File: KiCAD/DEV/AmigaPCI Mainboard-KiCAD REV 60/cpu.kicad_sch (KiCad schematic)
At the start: 55 parts, among them CN200 DIN41612_03x40, CN712 SPI, U712 ICE40HX4K-TQ144, U712F1 W25X20CLSN, U814 74LVC245, U816 74LVC245, U817 74LVC245

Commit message: APCI Rev 6.0 Work
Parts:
- added R277, R278: 2k7, Resistor_SMD:R_0603_1608Metric, symbol Device:R
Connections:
- net +3V3: now also R277.1, R278.1
- net _TBI: now also R278.2
- net _TEA: now also R277.2
- net _AWEN: now reaches U712.119 (IO0_178)
- no-connect marks 4 -> 3
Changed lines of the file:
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@@
 	(title_block
 		(title "AMIGA PCI")
-		(date "2025-04-24")
+		(date "2025-04-28")
 		(rev "6.0")
 	)
@@
 	)
 	(junction
+		(at 386.08 68.58)
+		(diameter 0)
+		(color 0 0 0 0)
+	)
+	(junction
 		(at 68.58 213.36)
 		(diameter 0)
@@
 	)
 	(junction
+		(at 388.62 68.58)
+		(diameter 0)
+		(color 0 0 0 0)
+	)
+	(junction
 		(at 393.7 68.58)
 		(diameter 0)
@@
 	)
 	(no_connect
-		(at 134.62 187.96)
-	)
-	(no_connect
 		(at 74.93 50.8)
 	)
@@
 	(wire
 		(pts
+			(xy 383.54 68.58) (xy 386.08 68.58)
+		)
+		(stroke
+			(width 0)
+			(type default)
+		)
+	)
+	(wire
+		(pts
 			(xy 44.45 210.82) (xy 53.34 210.82)
 		)
@@
 	(wire
 		(pts
+			(xy 383.54 88.9) (xy 383.54 82.55)
+		)
+		(stroke
+			(width 0)
+			(type default)
+		)
+	)
+	(wire
+		(pts
 			(xy 74.93 142.24) (xy 66.04 142.24)
 		)
@@
 	(wire
 		(pts
+			(xy 386.08 88.9) (xy 386.08 82.55)
+		)
+		(stroke
+			(width 0)
+			(type default)
+		)
+	)
+	(wire
+		(pts
 			(xy 129.54 43.18) (xy 129.54 45.72)
 		)
@@
 	(wire
 		(pts
+			(xy 386.08 68.58) (xy 386.08 74.93)
+		)
+		(stroke
+			(width 0)
+			(type default)
+		)
+	)
+	(wire
+		(pts
 			(xy 66.04 139.7) (xy 74.93 139.7)
 		)
@@
 	(wire
 		(pts
+			(xy 383.54 68.58) (xy 383.54 74.93)
+		)
+		(stroke
+			(width 0)
+			(type default)
+		)
+	)
+	(wire
+		(pts
 			(xy 312.42 157.48) (xy 311.15 157.48)
 		)
@@
 		)
 	)
+	(wire
+		(pts
+			(xy 386.08 68.58) (xy 388.62 68.58)
+		)
+		(stroke
+			(width 0)
+			(type default)
+		)
+	)
 	(bus
 		(pts
@@
 		)
 	)
+	(label "_TBI"
+		(at 383.54 88.9 90)
+		(effects
+			(font
+				(size 1.27 1.27)
+			)
+			(justify left bottom)
+		)
+	)
 	(label "D21"
 		(at 303.53 92.71 0)
@@
 		)
 	)
+	(label "_TEA"
+		(at 386.08 88.9 90)
+		(effects
+			(font
+				(size 1.27 1.27)
+			)
+			(justify left bottom)
+		)
+	)
 	(label "A23"
 		(at 328.93 57.15 0)
@@
 		)
 	)
+	(global_label "_AWEN"
+		(shape output)
+		(at 134.62 187.96 0)
+		(fields_autoplaced yes)
+		(effects
+			(font
+				(size 1.27 1.27)
+			)
+			(justify left)
+		)
+		(property "Intersheetrefs" "${INTERSHEET_REFS}"
+			(at 143.5923 187.96 0)
+			(effects
+				(font
+					(size 1.27 1.27)
+				)
+				(justify left)
+			)
+		)
+	)
 	(global_label "_BUSREQ1"
 		(shape output)
@@
 	)
 	(symbol
+		(lib_id "Device:R")
+		(at 386.08 78.74 0)
+		(mirror y)
+		(unit 1)
+		(exclude_from_sim no)
+		(in_bom yes)
+		(on_board yes)
+		(dnp no)
+		(property "Reference" "R277"
+			(at 384.81 75.692 90)
+			(effects
+				(font
+					(size 1.27 1.27)
+				)
+				(justify left)
+			)
+		)
+		(property "Value" "2k7"
+			(at 386.08 80.772 90)
+			(effects
+				(font
+					(size 1.27 1.27)
+				)
+				(justify left)
+			)
+		)
+		(property "Footprint" "Resistor_SMD:R_0603_1608Metric"
+			(at 387.858 78.74 90)
+			(effects
+				(font
+					(size 1.27 1.27)
+				)
+				(hide yes)
+			)
+		)
+		(property "Datasheet" "~"
+			(at 386.08 78.74 0)
+			(effects
+				(font
+					(size 1.27 1.27)
+				)
+				(hide yes)
+			)
+		)
+		(property "Description" ""
+			(at 386.08 78.74 0)
+			(effects
+				(font
+					(size 1.27 1.27)
+				)
+				(hide yes)
+			)
+		)
+		(pin "1"
+		)
+		(pin "2"
+		)
+		(instances
+			(project "AmigaPCI Mainboard"
+				(path "/72453515-27fe-4336-91f3-e3c8054f7767/14024e2c-eaac-4547-8875-4a8ac58b1720"
+					(reference "R277")
+					(unit 1)
+				)
+			)
+		)
+	)
+	(symbol
 		(lib_id "Device:R_Network08")
 		(at 339.09 90.17 270)
@@
 					(unit 1)
 				)
+			)
+		)
+	)
+	(symbol
+		(lib_id "Device:R")
+		(at 383.54 78.74 0)
+		(mirror y)
+		(unit 1)
+		(exclude_from_sim no)
+		(in_bom yes)
+		(on_board yes)
+		(dnp no)
+		(property "Reference" "R278"
+			(at 382.27 75.692 90)
+			(effects
+				(font
+					(size 1.27 1.27)
+				)
+				(justify left)
+			)
+		)
+		(property "Value" "2k7"
+			(at 383.54 80.772 90)
+			(effects
+				(font
+					(size 1.27 1.27)
+				)
+				(justify left)
+			)
+		)
+		(property "Footprint" "Resistor_SMD:R_0603_1608Metric"
+			(at 385.318 78.74 90)
+			(effects
+				(font
+					(size 1.27 1.27)
+				)
+				(hide yes)
+			)
+		)
+		(property "Datasheet" "~"
+			(at 383.54 78.74 0)
+			(effects
+				(font
+					(size 1.27 1.27)
+				)
+				(hide yes)
+			)
+		)
+		(property "Description" ""
+			(at 383.54 78.74 0)
+			(effects
+				(font
+					(size 1.27 1.27)
+				)
+				(hide yes)
+			)
+		)
+		(pin "1"
+		)
+		(pin "2"
+		)
+		(instances
+			(project "AmigaPCI Mainboard"
+				(path "/72453515-27fe-4336-91f3-e3c8054f7767/14024e2c-eaac-4547-8875-4a8ac58b1720"
+					(reference "R278")
+					(unit 1)
+				)

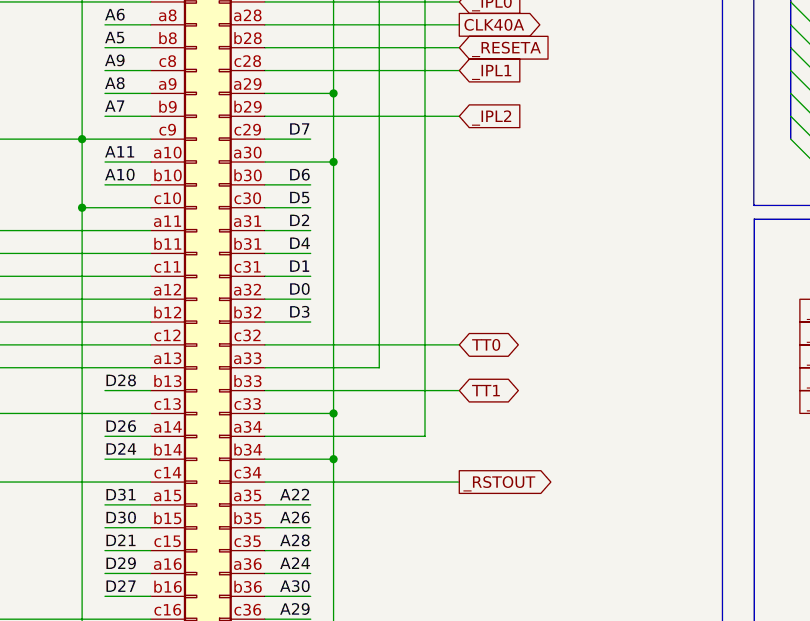
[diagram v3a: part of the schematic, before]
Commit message: Rev 6.0 APCI Work
Added ATA address lines to U110.
Cleaned up some routing.
Removed address lines from U109 - we can pick them up from the AD bus.
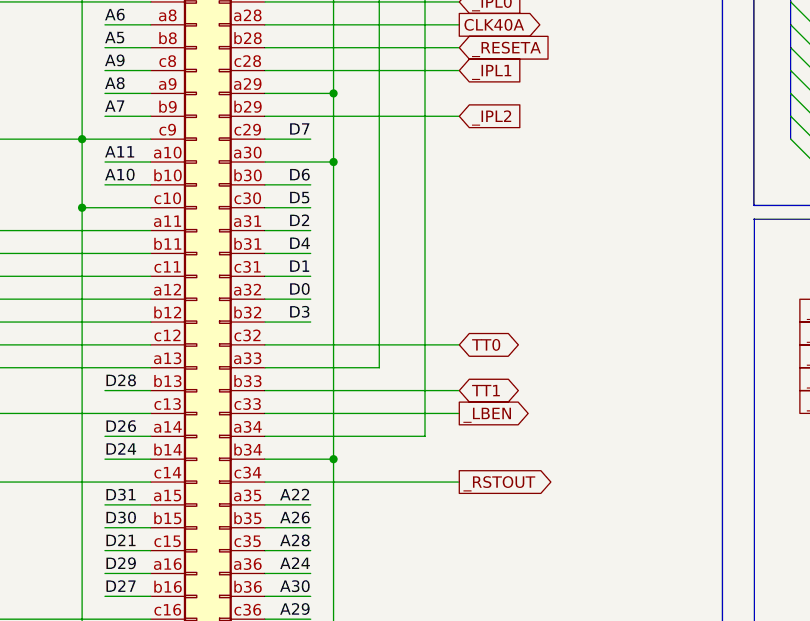
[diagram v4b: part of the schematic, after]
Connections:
- net GND: no longer CN200.c33 (Pin_c33)
- new net _LBEN: CN200.c33 (Pin_c33)
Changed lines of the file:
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@@
 	)
 	(junction
-		(at 250.19 146.05)
-		(diameter 0)
-		(color 0 0 0 0)
-	)
-	(junction
 		(at 375.92 38.1)
 		(diameter 0)
@@
 	(wire
 		(pts
-			(xy 250.19 146.05) (xy 250.19 151.13)
-		)
-		(stroke
-			(width 0)
-			(type default)
-		)
-	)
-	(wire
-		(pts
 			(xy 134.62 195.58) (xy 125.73 195.58)
 		)
@@
 	(wire
 		(pts
-			(xy 250.19 118.11) (xy 250.19 146.05)
+			(xy 250.19 118.11) (xy 250.19 151.13)
 		)
 		(stroke
@@
 	(wire
 		(pts
+			(xy 242.57 146.05) (xy 264.16 146.05)
+		)
+		(stroke
+			(width 0)
+			(type default)
+		)
+	)
+	(wire
+		(pts
 			(xy 134.62 180.34) (xy 125.73 180.34)
 		)
@@
 	(wire
 		(pts
-			(xy 242.57 146.05) (xy 250.19 146.05)
-		)
-		(stroke
-			(width 0)
-			(type default)
-		)
-	)
-	(wire
-		(pts
 			(xy 163.83 76.2) (xy 163.83 83.82)
 		)
@@
 			(effects
 				(font
+					(size 1.27 1.27)
+				)
+				(justify left)
+			)
+		)
+	)
+	(global_label "_LBEN"
+		(shape output)
+		(at 264.16 146.05 0)
+		(fields_autoplaced yes)
+		(effects
+			(font
+				(size 1.27 1.27)
+			)
+			(justify left)
+		)
+		(property "Intersheetrefs" "${INTERSHEET_REFS}"
+			(at 272.8904 146.05 0)
+			(effects
+				(font

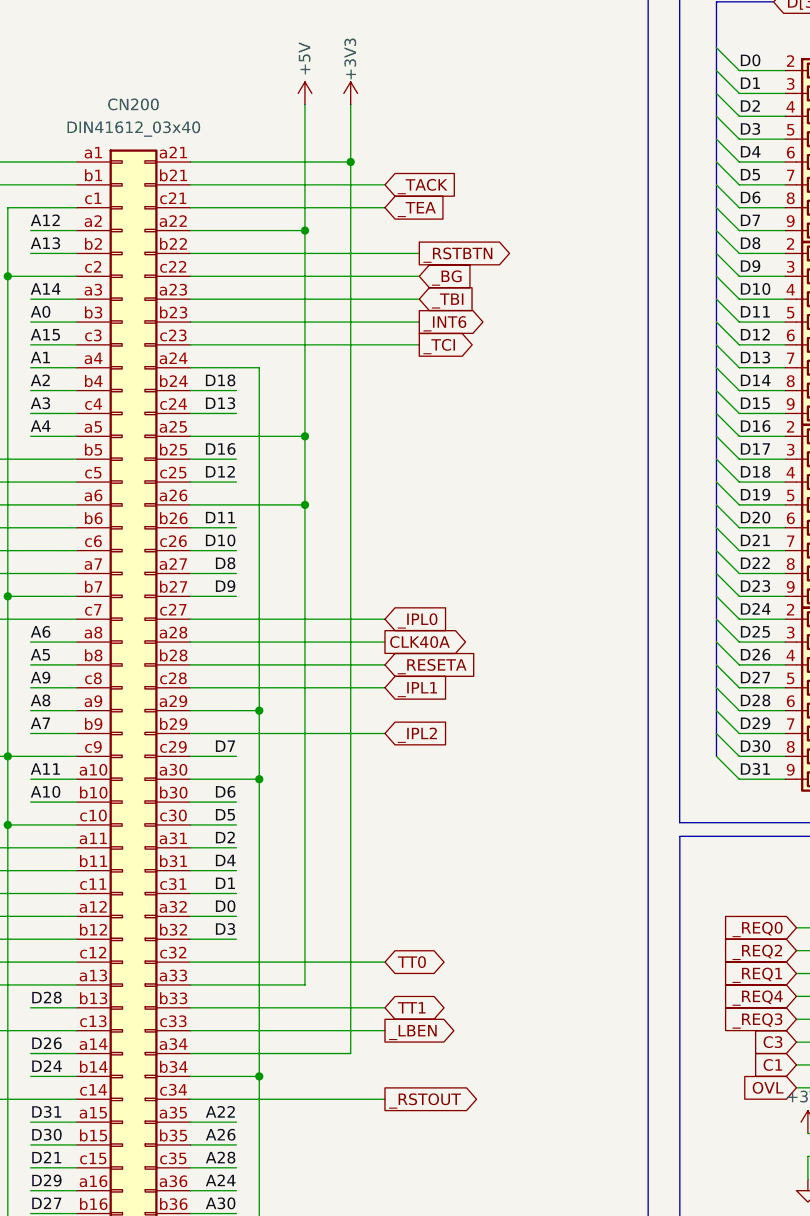
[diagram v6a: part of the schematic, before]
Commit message: APCI Added _LBEN pullup.
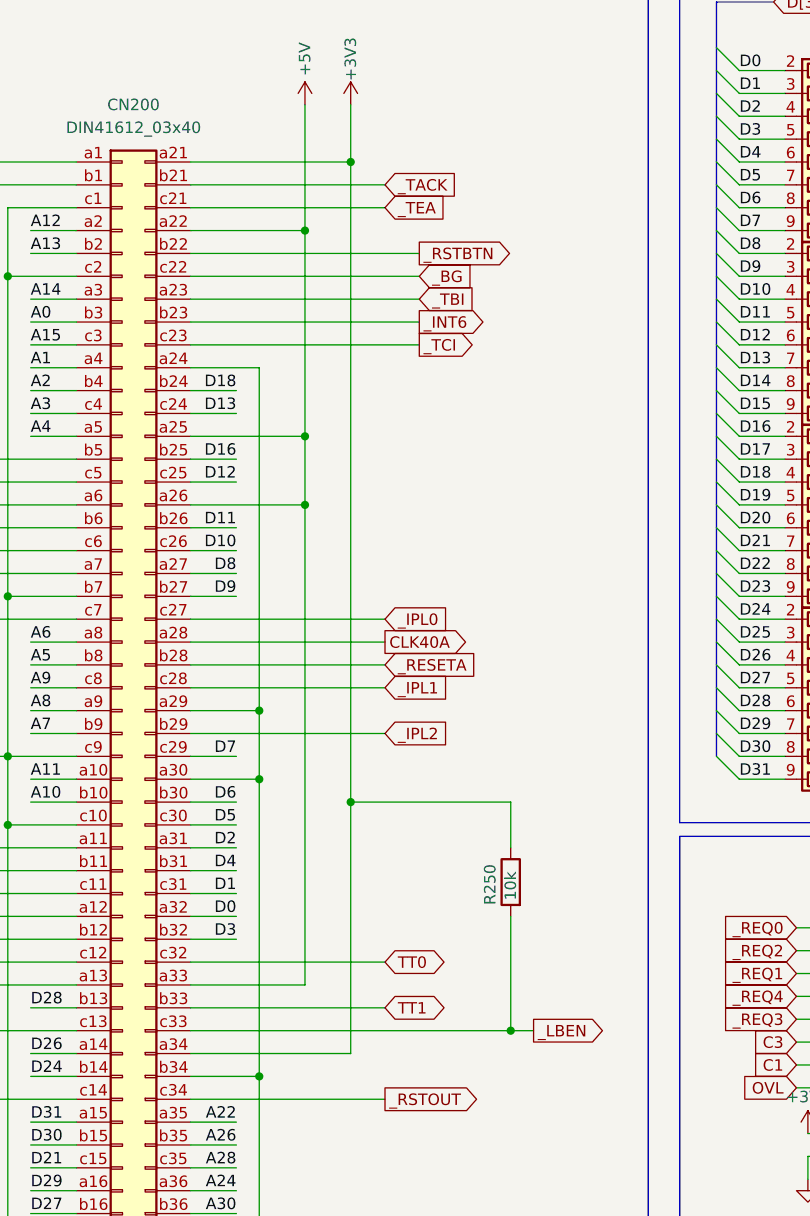
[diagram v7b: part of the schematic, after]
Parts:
- added R250: 10k, Resistor_SMD:R_0603_1608Metric, symbol Device:R
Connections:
- net +3V3: now also R250.1
- net _LBEN: now also R250.2
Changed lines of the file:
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@@
 	)
 	(junction
+		(at 260.35 120.65)
+		(diameter 0)
+		(color 0 0 0 0)
+	)
+	(junction
 		(at 151.13 50.8)
 		(diameter 0)
@@
 	)
 	(junction
+		(at 278.13 146.05)
+		(diameter 0)
+		(color 0 0 0 0)
+	)
+	(junction
 		(at 68.58 213.36)
 		(diameter 0)
@@
 		)
 	)
+	(wire
+		(pts
+			(xy 278.13 133.35) (xy 278.13 146.05)
+		)
+		(stroke
+			(width 0)
+			(type default)
+		)
+	)
 	(bus
 		(pts
@@
 	(wire
 		(pts
-			(xy 260.35 49.53) (xy 260.35 148.59)
+			(xy 260.35 49.53) (xy 260.35 120.65)
 		)
 		(stroke
@@
 	(wire
 		(pts
+			(xy 278.13 146.05) (xy 280.67 146.05)
+		)
+		(stroke
+			(width 0)
+			(type default)
+		)
+	)
+	(wire
+		(pts
 			(xy 242.57 118.11) (xy 250.19 118.11)
 		)
@@
 		)
 	)
+	(wire
+		(pts
+			(xy 278.13 125.73) (xy 278.13 120.65)
+		)
+		(stroke
+			(width 0)
+			(type default)
+		)
+	)
 	(bus
 		(pts
@@
 	(wire
 		(pts
+			(xy 260.35 120.65) (xy 260.35 148.59)
+		)
+		(stroke
+			(width 0)
+			(type default)
+		)
+	)
+	(wire
+		(pts
 			(xy 334.01 118.11) (xy 328.93 118.11)
 		)
@@
 	(wire
 		(pts
+			(xy 260.35 120.65) (xy 278.13 120.65)
+		)
+		(stroke
+			(width 0)
+			(type default)
+		)
+	)
+	(wire
+		(pts
 			(xy 242.57 87.63) (xy 255.27 87.63)
 		)
@@
 	(wire
 		(pts
-			(xy 242.57 146.05) (xy 264.16 146.05)
+			(xy 242.57 146.05) (xy 278.13 146.05)
 		)
 		(stroke
@@
 	(global_label "_LBEN"
 		(shape output)
-		(at 264.16 146.05 0)
+		(at 280.67 146.05 0)
 		(fields_autoplaced yes)
 		(effects
@@
 		)
 		(property "Intersheetrefs" "${INTERSHEET_REFS}"
-			(at 272.8904 146.05 0)
+			(at 289.4004 146.05 0)
 			(effects
 				(font
@@
 					(unit 1)
 				)
+			)
+		)
+	)
+	(symbol
+		(lib_id "Device:R")
+		(at 278.13 129.54 0)
+		(mirror y)
+		(unit 1)
+		(exclude_from_sim no)
+		(in_bom yes)
+		(on_board yes)
+		(dnp no)
+		(property "Reference" "R250"
+			(at 275.844 132.08 90)
+			(effects
+				(font
+					(size 1.27 1.27)
+				)
+				(justify left)
+			)
+		)
+		(property "Value" "10k"
+			(at 278.13 131.572 90)
+			(effects
+				(font
+					(size 1.27 1.27)
+				)
+				(justify left)
+			)
+		)
+		(property "Footprint" "Resistor_SMD:R_0603_1608Metric"
+			(at 279.908 129.54 90)
+			(effects
+				(font
+					(size 1.27 1.27)
+				)
+				(hide yes)
+			)
+		)
+		(property "Datasheet" "~"
+			(at 278.13 129.54 0)
+			(effects
+				(font
+					(size 1.27 1.27)
+				)
+				(hide yes)
+			)
+		)
+		(property "Description" ""
+			(at 278.13 129.54 0)
+			(effects
+				(font
+					(size 1.27 1.27)
+				)
+				(hide yes)
+			)
+		)
+		(pin "1"
+		)
+		(pin "2"
+		)
+		(instances
+			(project "AmigaPCI Mainboard"
+				(path "/72453515-27fe-4336-91f3-e3c8054f7767/14024e2c-eaac-4547-8875-4a8ac58b1720"
+					(reference "R250")
+					(unit 1)
+				)
